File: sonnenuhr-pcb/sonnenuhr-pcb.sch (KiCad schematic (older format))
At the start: 5 parts, among them J1 Conn_01x05_Male, J2 Conn_01x05_Male, U1 ULN2803A

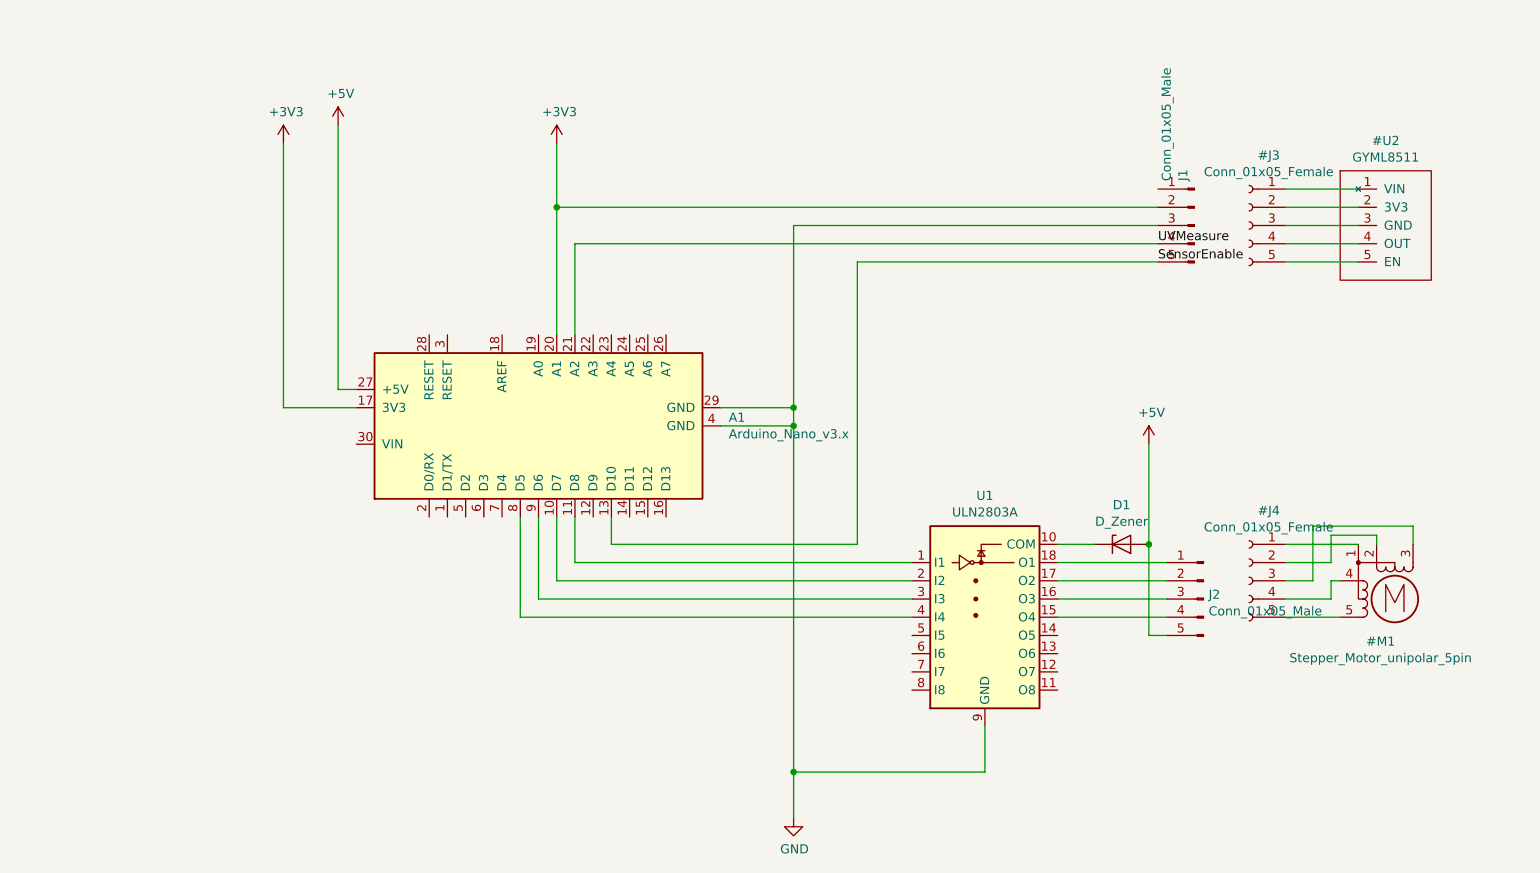
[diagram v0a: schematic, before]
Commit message: sonnenuhr-pcb: Add potentiometer
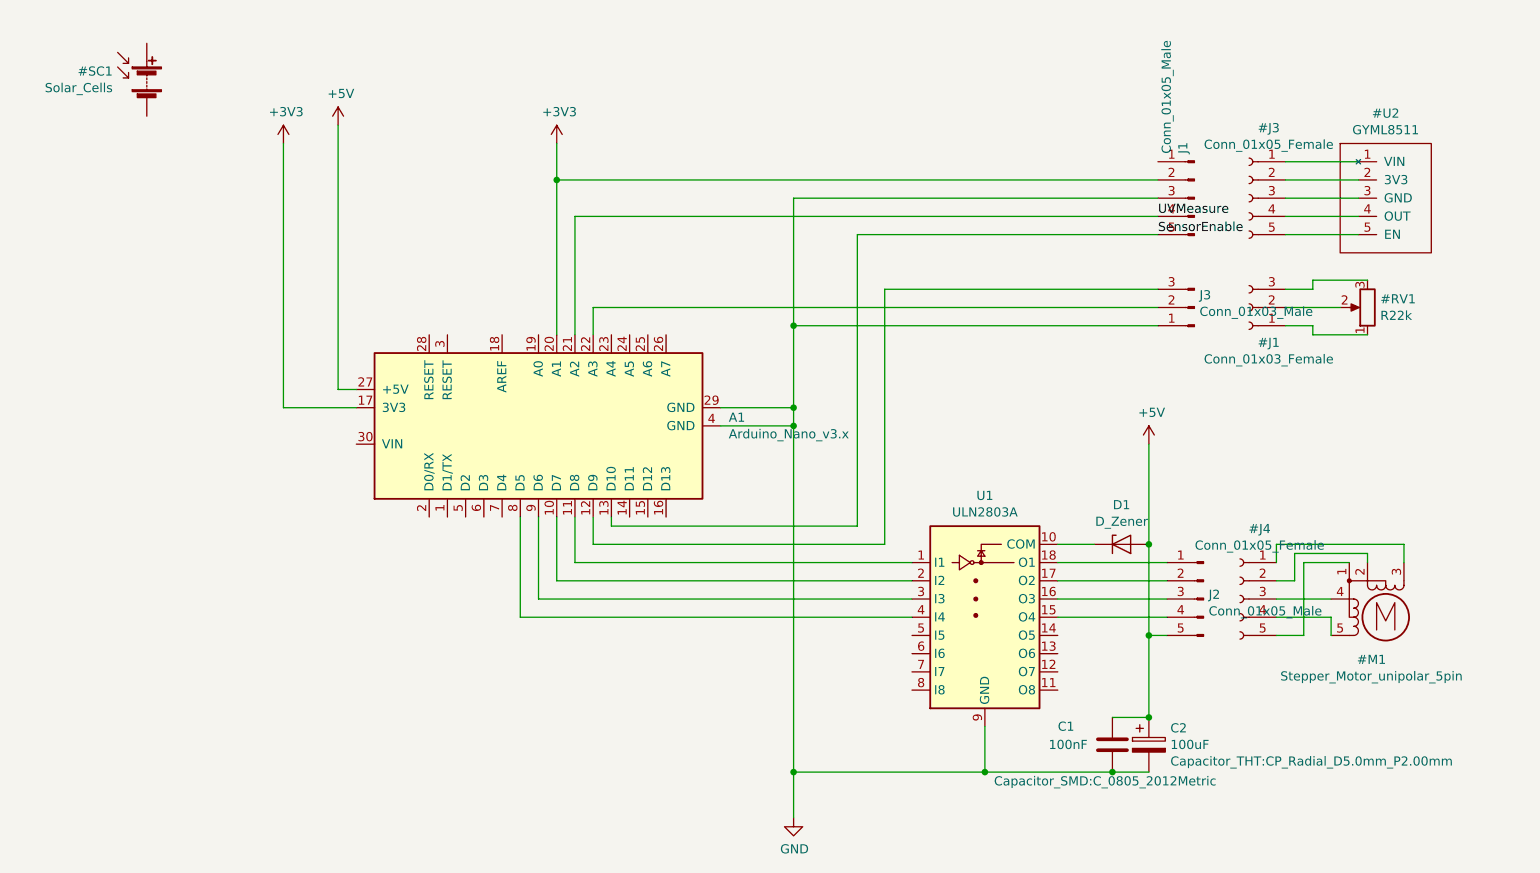
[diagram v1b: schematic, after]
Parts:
- added C1: 100nF, Capacitor_SMD:C_0805_2012Metric, symbol Device:C
- added C2: 100uF, Capacitor_THT:CP_Radial_D5.0mm_P2.00mm, symbol Device:CP
- added J3: Conn_01x03_Male, Connector_PinHeader_2.54mm:PinHeader_1x03_P2.54mm_Vertical, symbol Connector:Conn_01x03_Male
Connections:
- net +5V: now also C1.1, C2.1
- net GND: now also C1.2, C2.2, J3.1 (Pin_1)
- net at A1.12 (D9): now also J3.3 (Pin_3)
- net at A1.22 (A3): now also J3.2 (Pin_2)
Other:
- moved on the sheet: J1
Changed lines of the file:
@@
 EESchema Schematic File Version 4
+LIBS:sonnenuhr-pcb-cache
 EELAYER 29 0
 EELAYER END
@@
 L Motor:Stepper_Motor_unipolar_5pin #M1
 U 1 1 5CEAAF02
-P 8000 4000
-F 0 "#M1" H 7922 3767 50  0000 C CNN
-F 1 "Stepper_Motor_unipolar_5pin" H 7922 3676 50  0000 C CNN
-F 2 "" H 8010 3990 50  0001 C CNN
-F 3 "http://www.infineon.com/dgdl/Application-Note-TLE8110EE_driving_UniPolarStepperMotor_V1.1.pdf?fileId=db3a30431be39b97011be5d0aa0a00b0" H 8010 3990 50  0001 C CNN
-	1    8000 4000
+P 7950 4100
+F 0 "#M1" H 7872 3867 50  0000 C CNN
+F 1 "Stepper_Motor_unipolar_5pin" H 7872 3776 50  0000 C CNN
+F 2 "" H 7960 4090 50  0001 C CNN
+F 3 "http://www.infineon.com/dgdl/Application-Note-TLE8110EE_driving_UniPolarStepperMotor_V1.1.pdf?fileId=db3a30431be39b97011be5d0aa0a00b0" H 7960 4090 50  0001 C CNN
+	1    7950 4100
 	1    0    0    -1
 $EndComp
@@
 L Connector:Conn_01x05_Female #J4
 U 1 1 5CEAD4BD
-P 7200 3900
-F 0 "#J4" H 7092 4285 50  0000 C CNN
-F 1 "Conn_01x05_Female" H 7092 4194 50  0000 C CNN
-F 2 "Connector_PinSocket_2.54mm:PinSocket_1x05_P2.54mm_Vertical" H 7200 3900 50  0001 C CNN
-F 3 "~" H 7200 3900 50  0001 C CNN
-	1    7200 3900
+P 7150 4000
+F 0 "#J4" H 7042 4385 50  0000 C CNN
+F 1 "Conn_01x05_Female" H 7042 4294 50  0000 C CNN
+F 2 "Connector_PinSocket_2.54mm:PinSocket_1x05_P2.54mm_Vertical" H 7150 4000 50  0001 C CNN
+F 3 "~" H 7150 4000 50  0001 C CNN
+	1    7150 4000
 	-1   0    0    -1
 $EndComp
@@
 	1    0    0    -1
 $EndComp
-Wire Wire Line
-	7800 3700 7400 3700
-Wire Wire Line
-	7900 3700 7900 3650
-Wire Wire Line
-	7900 3650 7650 3650
-Wire Wire Line
-	7650 3650 7650 3800
-Wire Wire Line
-	7650 3800 7400 3800
-Wire Wire Line
-	8100 3700 8100 3600
-Wire Wire Line
-	8100 3600 7550 3600
-Wire Wire Line
-	7550 3600 7550 3900
-Wire Wire Line
-	7550 3900 7400 3900
-Wire Wire Line
-	7700 3900 7650 3900
-Wire Wire Line
-	7650 3900 7650 4000
-Wire Wire Line
-	7650 4000 7400 4000
-Wire Wire Line
-	7700 4100 7400 4100
 $Comp
 L sonnenuhr:GYML8511 #U2
 U 1 1 5CF0EBF5
-P 7700 1650
-F 0 "#U2" H 7950 1815 50  0000 C CNN
-F 1 "GYML8511" H 7950 1724 50  0000 C CNN
-F 2 "sonnenuhr-pcb:GYML8511" H 7700 1650 50  0001 C CNN
-F 3 "" H 7700 1650 50  0001 C CNN
-	1    7700 1650
+P 7700 1500
+F 0 "#U2" H 7950 1665 50  0000 C CNN
+F 1 "GYML8511" H 7950 1574 50  0000 C CNN
+F 2 "sonnenuhr-pcb:GYML8511" H 7700 1500 50  0001 C CNN
+F 3 "" H 7700 1500 50  0001 C CNN
+	1    7700 1500
 	1    0    0    -1
 $EndComp
@@
 L Connector:Conn_01x05_Female #J3
 U 1 1 5CF0FF59
-P 7200 1950
-F 0 "#J3" H 7092 2335 50  0000 C CNN
-F 1 "Conn_01x05_Female" H 7092 2244 50  0000 C CNN
-F 2 "Connector_PinSocket_2.54mm:PinSocket_1x05_P2.54mm_Vertical" H 7200 1950 50  0001 C CNN
-F 3 "~" H 7200 1950 50  0001 C CNN
-	1    7200 1950
+P 7200 1800
+F 0 "#J3" H 7092 2185 50  0000 C CNN
+F 1 "Conn_01x05_Female" H 7092 2094 50  0000 C CNN
+F 2 "Connector_PinSocket_2.54mm:PinSocket_1x05_P2.54mm_Vertical" H 7200 1800 50  0001 C CNN
+F 3 "~" H 7200 1800 50  0001 C CNN
+	1    7200 1800
 	-1   0    0    -1
 $EndComp
 Wire Wire Line
-	7400 1750 7800 1750
-Wire Wire Line
-	7400 1850 7800 1850
-Wire Wire Line
-	7400 1950 7800 1950
-Wire Wire Line
-	7400 2050 7800 2050
-Wire Wire Line
-	7400 2150 7800 2150
+	7400 1600 7800 1600
+Wire Wire Line
+	7400 1700 7800 1700
+Wire Wire Line
+	7400 1800 7800 1800
+Wire Wire Line
+	7400 1900 7800 1900
+Wire Wire Line
+	7400 2000 7800 2000
 $Comp
 L Connector:Conn_01x05_Male J1
 U 1 1 5CED387B
-P 6900 1950
-F 0 "J1" V 6962 2194 50  0000 L CNN
-F 1 "Conn_01x05_Male" V 7053 2194 50  0000 L CNN
-F 2 "Connector_PinHeader_2.54mm:PinHeader_1x05_P2.54mm_Horizontal" H 6900 1950 50  0001 C CNN
-F 3 "~" H 6900 1950 50  0001 C CNN
-	1    6900 1950
+P 6900 1800
+F 0 "J1" V 6962 2044 50  0000 L CNN
+F 1 "Conn_01x05_Male" V 7053 2044 50  0000 L CNN
+F 2 "Connector_PinHeader_2.54mm:PinHeader_1x05_P2.54mm_Horizontal" H 6900 1800 50  0001 C CNN
+F 3 "~" H 6900 1800 50  0001 C CNN
+	1    6900 1800
 	-1   0    0    -1
 $EndComp
 Wire Wire Line
-	6700 1850 3400 1850
-Wire Wire Line
-	3400 1850 3400 1500
+	6700 1700 3400 1700
+Wire Wire Line
+	3400 1700 3400 1500
 $Comp
 L power:+3V3 #PWR0105
@@
 $EndComp
 Wire Wire Line
-	6700 1950 4700 1950
-Wire Wire Line
-	6700 2150 5050 2150
-Wire Wire Line
-	5050 2150 5050 3700
+	6700 1800 4700 1800
+Wire Wire Line
+	6700 2000 5050 2000
+Wire Wire Line
+	5050 2000 5050 3600
 Wire Wire Line
 	4300 3050 4700 3050
@@
 	4700 2950 4700 3050
 Wire Wire Line
-	4700 1950 4700 2950
+	4700 1800 4700 2500
 Connection ~ 4700 2950
 Wire Wire Line
@@
 Connection ~ 4700 4950
 Wire Wire Line
-	6700 2050 3500 2050
-Wire Wire Line
-	3500 2050 3500 2550
-Connection ~ 3400 1850
-Wire Wire Line
-	3400 1850 3400 2550
+	6700 1900 3500 1900
+Wire Wire Line
+	3500 1900 3500 2550
+Connection ~ 3400 1700
+Wire Wire Line
+	3400 1700 3400 2550
 Wire Wire Line
 	1900 1500 1900 2950
@@
 	3500 3800 5350 3800
 Wire Wire Line
-	3700 3700 3700 3550
-Wire Wire Line
-	3700 3700 5050 3700
-Text Label 6700 2050 0    50   ~ 0
+	3700 3600 3700 3550
+Wire Wire Line
+	3700 3600 5050 3600
+Text Label 6700 1900 0    50   ~ 0
 UVMeasure
-Text Label 6700 2150 0    50   ~ 0
+Text Label 6700 2000 0    50   ~ 0
 SensorEnable
+Wire Wire Line
+	7350 4200 7500 4200
+Wire Wire Line
+	7500 4200 7500 3800
+Wire Wire Line
+	7500 3800 7750 3800
+Wire Wire Line
+	7350 3900 7450 3900
+Wire Wire Line
+	7450 3900 7450 3750
+Wire Wire Line
+	7450 3750 7850 3750
+Wire Wire Line
+	7850 3750 7850 3800
+Wire Wire Line
+	7350 3800 7350 3700
+Wire Wire Line
+	7350 3700 8050 3700
+Wire Wire Line
+	8050 3700 8050 3800
+Wire Wire Line
+	7350 4000 7650 4000
+Wire Wire Line
+	7350 4100 7650 4100
+Wire Wire Line
+	7650 4100 7650 4200
+$Comp
+L Device:CP C2
+U 1 1 5CEED029
+P 6650 4800
+F 0 "C2" H 6768 4891 50  0000 L CNN
+F 1 "100uF" H 6768 4800 50  0000 L CNN
+F 2 "Capacitor_THT:CP_Radial_D5.0mm_P2.00mm" H 6768 4709 50  0000 L CNN
+F 3 "~" H 6650 4800 50  0001 C CNN
+	1    6650 4800
+	1    0    0    -1
+$EndComp
+Wire Wire Line
+	6650 4200 6650 4650
+Connection ~ 6650 4200
+Wire Wire Line
+	6650 4650 6450 4650
+Connection ~ 6650 4650
+Wire Wire Line
+	6650 4950 6450 4950
+Connection ~ 5750 4950
+Connection ~ 6450 4950
+Wire Wire Line
+	6450 4950 5750 4950
+$Comp
+L Device:C C1
+U 1 1 5CEED474
+P 6450 4800
+F 0 "C1" H 6150 4900 50  0000 L CNN
+F 1 "100nF" H 6100 4800 50  0000 L CNN
+F 2 "Capacitor_SMD:C_0805_2012Metric" H 5800 4600 50  0000 L CNN
+F 3 "~" H 6450 4800 50  0001 C CNN
+	1    6450 4800
+	1    0    0    -1
+$EndComp
+$Comp
+L Device:Solar_Cells #SC1
+U 1 1 5CEFF7B1
+P 1150 1150
+F 0 "#SC1" H 963 1196 50  0000 R CNN
+F 1 "Solar_Cells" H 963 1105 50  0000 R CNN
+F 2 "" V 1150 1210 50  0001 C CNN
+F 3 "~" V 1150 1210 50  0001 C CNN
+	1    1150 1150
+	1    0    0    -1
+$EndComp
+$Comp
+L Device:R_POT #RV1
+U 1 1 5CF06F42
+P 7850 2400
+F 0 "#RV1" H 7780 2354 50  0000 R CNN
+F 1 "R22k" H 7780 2445 50  0000 R CNN
+F 2 "" H 7850 2400 50  0001 C CNN
+F 3 "~" H 7850 2400 50  0001 C CNN
+	1    7850 2400
+	-1   0    0    1
+$EndComp
+$Comp
+L Connector:Conn_01x03_Female #J1
+U 1 1 5CF0AE95
+P 7200 2400
+F 0 "#J1" H 7092 2593 50  0000 C CNN
+F 1 "Conn_01x03_Female" H 7092 2684 50  0000 C CNN
+F 2 "" H 7200 2400 50  0001 C CNN
+F 3 "~" H 7200 2400 50  0001 C CNN
+	1    7200 2400
+	-1   0    0    1
+$EndComp
+$Comp
+L Connector:Conn_01x03_Male J3
+U 1 1 5CF0BB94
+P 6900 2400
+F 0 "J3" H 6872 2332 50  0000 R CNN
+F 1 "Conn_01x03_Male" H 6872 2423 50  0000 R CNN
+F 2 "Connector_PinHeader_2.54mm:PinHeader_1x03_P2.54mm_Vertical" H 6900 2400 50  0001 C CNN
+F 3 "~" H 6900 2400 50  0001 C CNN
+	1    6900 2400
+	-1   0    0    1
+$EndComp
+Wire Wire Line
+	7400 2300 7550 2300
+Wire Wire Line
+	7550 2300 7550 2250
+Wire Wire Line
+	7550 2250 7850 2250
+Wire Wire Line
+	7400 2400 7700 2400
+Wire Wire Line
+	7400 2500 7550 2500
+Wire Wire Line
+	7550 2500 7550 2550
+Wire Wire Line
+	7550 2550 7850 2550
+Wire Wire Line
+	3600 3550 3600 3700
+Wire Wire Line
+	3600 3700 5200 3700
+Wire Wire Line
+	5200 3700 5200 2300
+Wire Wire Line
+	5200 2300 6700 2300
+Wire Wire Line
+	6700 2400 3600 2400
+Wire Wire Line
+	3600 2400 3600 2550
+Wire Wire Line
+	6700 2500 4700 2500
+Connection ~ 4700 2500
+Wire Wire Line
+	4700 2500 4700 2950
 $EndSCHEMATC
